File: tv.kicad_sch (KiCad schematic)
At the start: 49 parts, among them IC1 CXA1145, IC29 74HC4024, IC30 74HC10, U1 Analog Video breakout, X1 4.433619MHz

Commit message: prepare for fabrication
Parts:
- C221, C23, C31: LCSC (none) -> C344201; LCSC Part (none) -> C344201
- C26: LCSC (none) -> C107115; LCSC Part (none) -> C107115
- C32, C34, C35, C36: LCSC (none) -> C49678; LCSC Part (none) -> C49678
- IC29: LCSC (none) -> C2652991; LCSC Part (none) -> C2652991
- IC30: LCSC (none) -> C6816; LCSC Part (none) -> C6816
- R10, R11, R13, R224: LCSC (none) -> C17477; LCSC Part (none) -> C17477
- R12: LCSC (none) -> C844020; LCSC Part (none) -> C844020
- R14, R15, R20, R21: LCSC (none) -> C2907232; LCSC Part (none) -> C2907232
- R19: LCSC (none) -> C422599; LCSC Part (none) -> C422599
- R210: LCSC (none) -> C54102237; LCSC Part (none) -> C54102237
- R211: LCSC (none) -> C2930266; LCSC Part (none) -> C2930266
- R214: LCSC (none) -> C2907219; LCSC Part (none) -> C2907219
- R7: LCSC (none) -> C2960740; LCSC Part (none) -> C2960740
- R8: LCSC (none) -> C114929; LCSC Part (none) -> C114929
- R9: LCSC (none) -> C2933528; LCSC Part (none) -> C2933528
- TP30, TP31, TP32, TP36, TP37, TP38, TP39, TP40, TP42: now not fitted

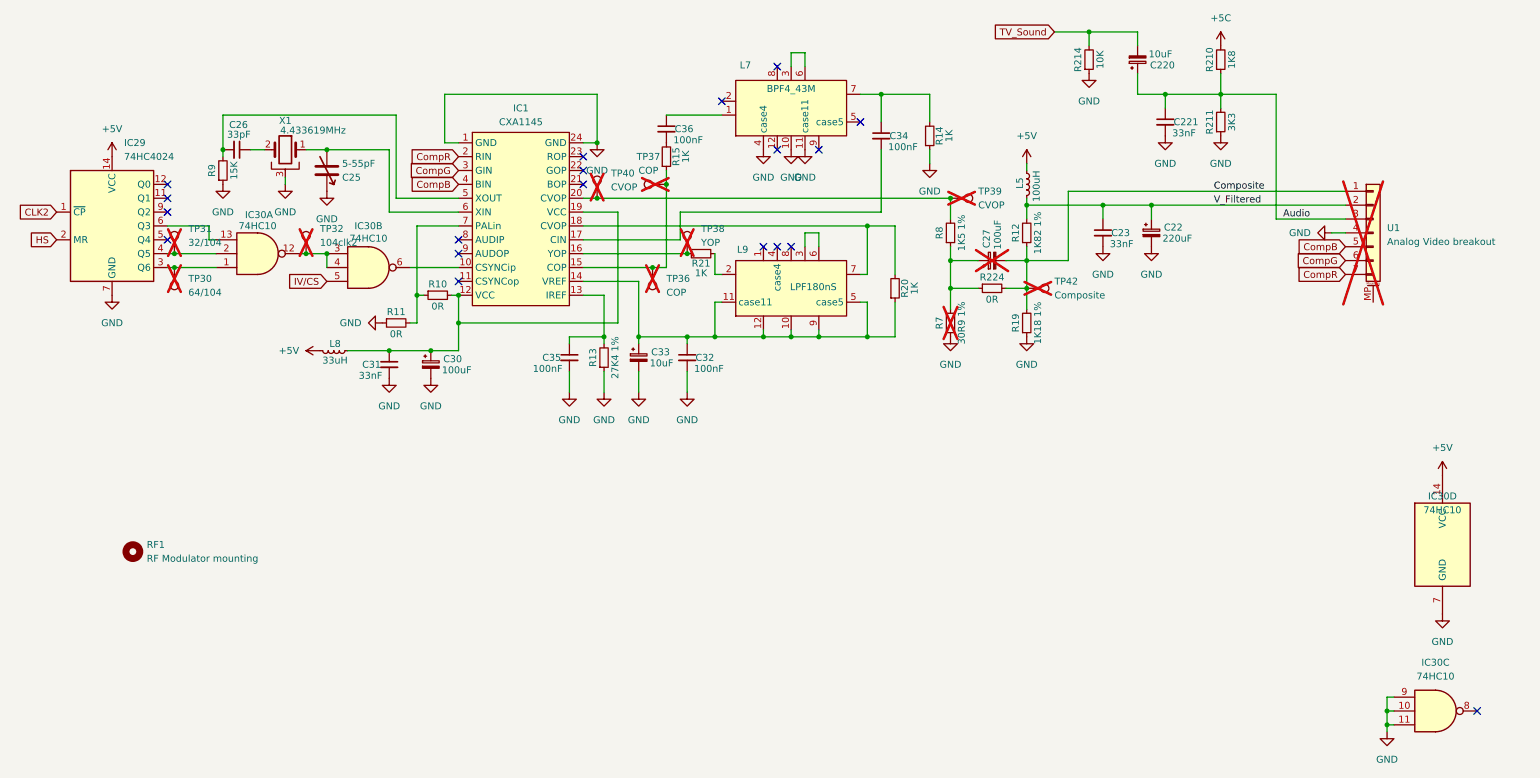
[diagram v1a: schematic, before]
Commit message: verify all component values vs TRM
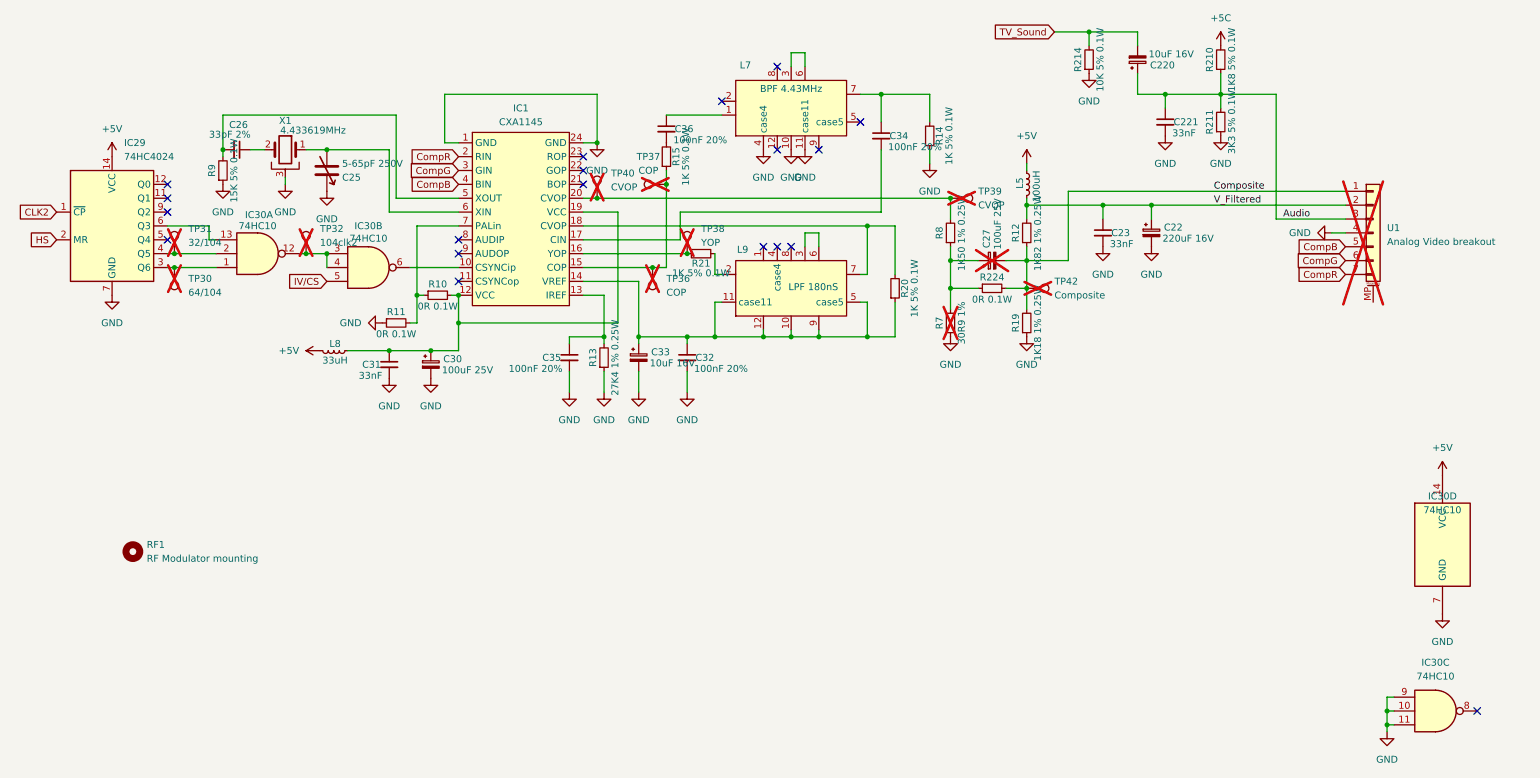
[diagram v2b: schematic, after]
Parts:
- C22: value 220uF -> 220uF 16V
- C220, C33: value 10uF -> 10uF 16V
- C25: value 5-55pF -> 5-65pF 250V
- C26: value 33pF -> 33pF 2%
- C27, C30: value 100uF -> 100uF 25V
- C32, C34, C35, C36: value 100nF -> 100nF 20%
- L7: value BPF4_43M -> BPF 4.43MHz
- L9: value LPF180nS -> LPF 180nS
- R10, R11, R224: value 0R -> 0R 0.1W
- R12: value 1K82 1% -> 1K82 1% 0.25W
- R13: value 27K4 1% -> 27K4 1% 0.25W; footprint Resistor_SMD:R_0805_2012Metric -> Resistor_SMD:R_1206_3216Metric
- R14, R15, R20, R21: value 1K -> 1K 5% 0.1W
- R19: value 1K18 1% -> 1K18 1% 0.25W
- R210: value 1K8 -> 1K8 5% 0.1W
- R211: value 3K3 -> 3K3 5% 0.1W
- R214: value 10K -> 10K 5% 0.1W
- R8: value 1K5 1% -> 1K50 1% 0.25W
- R9: value 15K -> 15K 5% 0.1W
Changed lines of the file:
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@@
 			)
 		)
-		(property "Value" "LPF180nS"
+		(property "Value" "LPF 180nS"
 			(at 159.004 79.756 90)
 			(effects
@@
 			)
 		)
-		(property "Value" "1K82 1%"
+		(property "Value" "1K82 1% 0.25W"
 			(at 200.152 69.85 90)
 			(effects
@@
 			)
 		)
-		(property "Value" "10K"
+		(property "Value" "10K 5% 0.1W"
 			(at 211.582 38.1 90)
 			(effects
@@
 			)
 		)
-		(property "Value" "0R"
+		(property "Value" "0R 0.1W"
 			(at 90.17 83.312 90)
 			(effects
@@
 			)
 		)
-		(property "Value" "0R"
+		(property "Value" "0R 0.1W"
 			(at 191.77 82.042 90)
 			(effects
@@
 			)
 		)
-		(property "Value" "1K"
+		(property "Value" "1K 5% 0.1W"
 			(at 177.546 80.01 90)
 			(effects
@@
 			)
 		)
-		(property "Value" "100uF"
+		(property "Value" "100uF 25V"
 			(at 90.932 94.996 0)
 			(effects
@@
 			)
 		)
-		(property "Value" "BPF4_43M"
+		(property "Value" "BPF 4.43MHz"
 			(at 154.94 43.434 90)
 			(effects
@@
 			)
 		)
-		(property "Value" "1K5 1%"
+		(property "Value" "1K50 1% 0.25W"
 			(at 186.182 69.85 90)
 			(effects
@@
 			)
 		)
-		(property "Value" "3K3"
+		(property "Value" "3K3 5% 0.1W"
 			(at 235.712 49.53 90)
 			(effects
@@
 			)
 		)
-		(property "Value" "1K18 1%"
+		(property "Value" "1K18 1% 0.25W"
 			(at 200.152 86.36 90)
 			(effects
@@
 			)
 		)
-		(property "Value" "27K4 1%"
+		(property "Value" "27K4 1% 0.25W"
 			(at 122.682 92.71 90)
 			(effects
@@
 			)
 		)
-		(property "Footprint" "Resistor_SMD:R_0805_2012Metric"
+		(property "Footprint" "Resistor_SMD:R_1206_3216Metric"
 			(at 120.65 92.71 0)
 			(effects
@@
 			)
 		)
-		(property "Value" "1K"
+		(property "Value" "1K 5% 0.1W"
 			(at 183.896 52.07 90)
 			(effects
@@
 			)
 		)
-		(property "Value" "10uF"
+		(property "Value" "10uF 16V"
 			(at 129.032 93.726 0)
 			(effects
@@
 			)
 		)
-		(property "Value" "100nF"
+		(property "Value" "100nF 20%"
 			(at 113.03 94.742 0)
 			(effects
@@
 			)
 		)
-		(property "Value" "100nF"
+		(property "Value" "100nF 20%"
 			(at 133.35 52.832 0)
 			(effects
@@
 			)
 		)
-		(property "Value" "10uF"
+		(property "Value" "10uF 16V"
 			(at 220.472 37.084 0)
 			(effects
@@
 			)
 		)
-		(property "Value" "100nF"
+		(property "Value" "100nF 20%"
 			(at 137.16 94.742 0)
 			(effects
@@
 			)
 		)
-		(property "Value" "100nF"
+		(property "Value" "100nF 20%"
 			(at 172.72 54.102 0)
 			(effects
@@
 			)
 		)
-		(property "Value" "0R"
+		(property "Value" "0R 0.1W"
 			(at 82.55 88.392 90)
 			(effects
@@
 			)
 		)
-		(property "Value" "15K"
+		(property "Value" "15K 5% 0.1W"
 			(at 52.832 58.42 90)
 			(effects
@@
 			)
 		)
-		(property "Value" "1K8"
+		(property "Value" "1K8 5% 0.1W"
 			(at 235.712 38.1 90)
 			(effects
@@
 			)
 		)
-		(property "Value" "1K"
+		(property "Value" "1K 5% 0.1W"
 			(at 138.43 77.216 90)
 			(effects
@@
 			)
 		)
-		(property "Value" "220uF"
+		(property "Value" "220uF 16V"
 			(at 223.012 70.866 0)
 			(effects
@@
 			)
 		)
-		(property "Value" "1K"
+		(property "Value" "1K 5% 0.1W"
 			(at 135.636 55.88 90)
 			(effects
@@
 			)
 		)
-		(property "Value" "100uF"
+		(property "Value" "100uF 25V"
 			(at 192.786 72.898 0)
 			(effects
@@
 			)
 		)
-		(property "Value" "33pF"
+		(property "Value" "33pF 2%"
 			(at 55.88 51.816 90)
 			(effects
@@
 			)
 		)
-		(property "Value" "5-55pF"
+		(property "Value" "5-65pF 250V"
 			(at 72.644 57.15 0)
 			(effects

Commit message: fix power domain links with net ties
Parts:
- U1: footprint Connector_PinSocket_2.54mm:PinSocket_1x07_P2.54mm_Vertical -> Connector_PinSocket_2.54mm:PinSocket_1x08_P2.54mm_Vertical; symbol Connector_Generic_MountingPin:Conn_01x07_MountingPin -> Connector_Generic:Conn_01x08
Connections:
- net CSync: now reaches IC1.10 (CSYNCip), IC30.6
- net CSync: now also U1.8 (Pin_8)
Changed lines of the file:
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@@
 	(wire
 		(pts
+			(xy 246.38 80.01) (xy 256.54 80.01)
+		)
+		(stroke
+			(width 0)
+			(type default)
+		)
+	)
+	(wire
+		(pts
 			(xy 198.12 57.15) (xy 198.12 58.42)
 		)
@@
 		)
 	)
+	(label "CSync"
+		(at 246.38 80.01 180)
+		(effects
+			(font
+				(size 1.27 1.27)
+			)
+			(justify right bottom)
+		)
+	)
 	(label "Composite"
 		(at 232.41 62.23 0)
@@
 		)
 	)
+	(label "CSync"
+		(at 85.09 76.2 0)
+		(effects
+			(font
+				(size 1.27 1.27)
+			)
+			(justify left bottom)
+		)
+	)
 	(global_label "IV{slash}CS"
 		(shape input)
@@
 	)
 	(symbol
-		(lib_id "Connector_Generic_MountingPin:Conn_01x07_MountingPin")
+		(lib_id "Connector_Generic:Conn_01x08")
 		(at 261.62 69.85 0)
 		(unit 1)
@@
 		(fields_autoplaced yes)
 		(property "Reference" "U1"
-			(at 264.16 68.9355 0)
+			(at 264.16 69.8499 0)
 			(effects
 				(font
@@
 		)
 		(property "Value" "Analog Video breakout"
-			(at 264.16 71.4755 0)
+			(at 264.16 72.3899 0)
 			(effects
 				(font
@@
 			)
 		)
-		(property "Footprint" "Connector_PinSocket_2.54mm:PinSocket_1x07_P2.54mm_Vertical"
+		(property "Footprint" "Connector_PinSocket_2.54mm:PinSocket_1x08_P2.54mm_Vertical"
 			(at 261.62 69.85 0)
 			(effects
@@
 			)
 		)
-		(property "Description" "Generic connectable mounting pin connector, single row, 01x07, script generated (kicad-library-utils/schlib/autogen/connector/)"
+		(property "Description" "Generic connector, single row, 01x08, script generated (kicad-library-utils/schlib/autogen/connector/)"
 			(at 261.62 69.85 0)
 			(effects
@@
 		(pin "7"
 		)
-		(pin "MP"
+		(pin "8"
 		)
 		(instances

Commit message: fix power and cmposite output
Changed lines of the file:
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@@
 	(generator_version "9.0")
 	(paper "A4")
+	(text_box "To use modulator replacement omit all components on this page except for IC29, IC30, L5, C23 and C22\n\nIf parts are already fitted, R12 must be removed"
+		(exclude_from_sim no)
+		(at 209.55 91.44 0)
+		(size 41.91 15.24)
+		(margins 0.9525 0.9525 0.9525 0.9525)
+		(stroke
+			(width 0)
+			(type solid)
+		)
+		(fill
+			(type none)
+		)
+		(effects
+			(font
+				(size 1.27 1.27)
+			)
+			(justify left top)
+		)
+	)
 	(junction
 		(at 88.9 91.44)

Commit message: fix incorrect footprint size for C22
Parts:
- C22: footprint Capacitor_THT:CP_Radial_D5.0mm_P2.50mm -> Capacitor_THT:CP_Radial_D8.0mm_P5.00mm
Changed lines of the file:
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@@
 			)
 		)
-		(property "Footprint" "Capacitor_THT:CP_Radial_D5.0mm_P2.50mm"
+		(property "Footprint" "Capacitor_THT:CP_Radial_D8.0mm_P5.00mm"
 			(at 220.98 69.85 0)
 			(effects

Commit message: modify RF footprint and add original signal hookup points
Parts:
- removed TP42: Composite, TestPoint:TestPoint_Pad_D1.0mm, symbol Connector:TestPoint
- added JV1: Composite, Connector_PinHeader_2.54mm:PinHeader_1x01_P2.54mm_Vertical, symbol Connector_Generic:Conn_01x01
- added JV2: Audio, Connector_PinHeader_2.54mm:PinHeader_1x01_P2.54mm_Vertical, symbol Connector_Generic:Conn_01x01
- added JV3: V_Filtered, Connector_PinHeader_2.54mm:PinHeader_1x01_P2.54mm_Vertical, symbol Connector_Generic:Conn_01x01
- RF1: symbol Mechanical:MountingHole -> Mechanical:MountingHole_Pad
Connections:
- net Audio: now also JV2.1 (Pin_1)
- net Composite: now also JV1.1 (Pin_1)
- net GND: now also RF1.1
- net V_Filtered: now also JV3.1 (Pin_1)

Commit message: enforce net class on AC
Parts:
- X1: footprint Crystal:Crystal_HC50_Horizontal_1EP_style2 -> Crystal:Crystal_HC49-U_Horizontal_1EP_style2
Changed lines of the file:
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@@
 			)
 		)
-		(property "Footprint" "Crystal:Crystal_HC50_Horizontal_1EP_style2"
+		(property "Footprint" "Crystal:Crystal_HC49-U_Horizontal_1EP_style2"
 			(at 62.23 54.61 0)
 			(effects
